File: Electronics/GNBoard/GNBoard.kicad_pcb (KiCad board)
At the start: 2 copper layers, 77.9 x 54.5 mm, 47 parts, among them K1 IR1, K10 IR4, K11 CNY_1, K12 CNY_2, K13 CNY_3, K14 CNY_4, K15 CNY_5, K16 CNY_6, K2 IR2, K3 SERVO_1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

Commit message: Working in new version for the GNBoard
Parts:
- removed K15: CNY_5, PIN_ARRAY_3X1
- removed K16: CNY_6, PIN_ARRAY_3X1
- removed P5: I2C_2, PIN_ARRAY_4x1
- added K17: Nose, PIN_ARRAY_3X1, F.Cu at (125.9, 92.8)
- added M1: XBEE, xbee_r1-XBEE, F.Cu at (117.0, 50.9)
- added R13: 10k, R3-LARGE_PADS, F.Cu at (128.4, 100.5)
- added R14: 10k, R3-LARGE_PADS, F.Cu at (123.3, 100.5)
- added R15: 4k7, R3-LARGE_PADS, F.Cu at (120.1, 43.4)
- added R16: 4k7, R3-LARGE_PADS, F.Cu at (120.1, 46.1)
- added R17: 7k5, R3-LARGE_PADS, F.Cu at (120.1, 48.8)
- added R18: 99k, R3-LARGE_PADS, F.Cu at (65.8, 42.2)
- C1: footprint C1V5 -> C1V8
- L1: footprint Choke_Toroid_6,5x13mm_Vertical -> Choke_Toroid_8x16mm_Vertical
- LED1: footprint LED5_RGB_long_wide -> LED5_RGB_long
- R1: value 6k8 -> 62k
- R5: value 6k8 -> 20k
- SHIELD1: footprint ARDUINO_MEGA_SHIELD -> ARDUINO_MEGA_SHIELD_MOD
- SW1: footprint SWITCH_3Pin -> switch_power_custom
- moved C4 120.6 mm to (64.6, 47.1)
- moved C5 99.2 mm to (108.0, 35.1)
- moved C2 98.8 mm to (72.6, 57.4), turned to 90 degrees
- moved LED1 94.8 mm to (62.6, 37.5), turned to 0 degrees
- moved SW3 88.9 mm to (54.1, 73.3)
- moved R2 88.9 mm to (70.6, 33.0), turned to 180 degrees
- moved SW1 88.8 mm to (55.6, 62.4)
- moved K11 88.6 mm to (95.4, 36.7)
- moved K12 88.6 mm to (97.9, 36.7)
- moved K13 88.6 mm to (100.5, 36.7)
- moved K14 88.6 mm to (103.0, 36.7)
- moved D1 88.6 mm to (68.2, 63.5)
- moved SW2 88.1 mm to (55.8, 42.0)
- moved R11 87.3 mm to (120.1, 32.9)
- moved P1 87.3 mm to (55.8, 54.0)
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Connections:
- C5 pad 1: +5V -> +3.3V
- P3 pad 2: GND -> N-0000043
- P6 pad 3: N-0000082 -> (no net)
- SHIELD1 pad 13: N-0000067 -> (no net)
- SHIELD1 pad 18: CNY5 -> XB_DIN
- SHIELD1 pad 19: CNY6 -> XB_DOUT
- SHIELD1 pad 3V3: N-0000040 -> +3.3V
- SHIELD1 pad AD10: N-0000041 -> Nose_V
- SHIELD1 pad AD11: N-0000039 -> (no net)
- SHIELD1 pad AD12: N-0000042 -> (no net)
- SHIELD1 pad AD13: N-0000043 -> (no net)
- SHIELD1 pad AD14: N-0000044 -> (no net)
- SHIELD1 pad AD15: N-0000045 -> (no net)
- SHIELD1 pad AREF: N-0000037 -> (no net)
- SHIELD1 pad V_IN: N-0000038 -> (no net)
- SW1 pad 3: N-0000046 -> (no net)
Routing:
- net GND: track 352.1 -> 36.9 mm, vias 4 -> 0
- net +5V: track 208.7 -> 43.3 mm
- net LDR4: track 39.0 -> 0.00 mm
- net LDR3: track 36.5 -> 0.00 mm
- net LDR2: track 33.9 -> 0.00 mm
- net XB_DOUT: track 0.00 -> 31.8 mm
- net LDR1: track 31.4 -> 0.00 mm
- net XB_DIN: track 0.00 -> 28.3 mm
- net BattVolt: track 44.8 -> 18.7 mm
- net +3.3V: track 0.00 -> 18.8 mm
- net Button1: track 5.50 -> 21.8 mm
- net ResetB: track 5.13 -> 20.8 mm
- net DHTpin: track 14.1 -> 0.00 mm
- net +BATT: track 28.9 -> 40.5 mm
- net N-0000034: track 0.00 -> 11.2 mm
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- added copper zone on F.Cu, net +5V
- added copper zone on B.Cu, net GND
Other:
- board size 77.9 x 54.5 mm -> 80 x 55.9 mm
- net class Default: clearance 0.4 -> 0.3; trace_width 0.8 -> 0.4; via_dia 1.5 -> 0.889; via_drill 0.6 -> 0.508
- rule trace_clearance: 0.4 -> 0.3
- board text added: "GNBoard v0.2"
- board text removed: "GNBoard"
- board text removed: "v0.1"

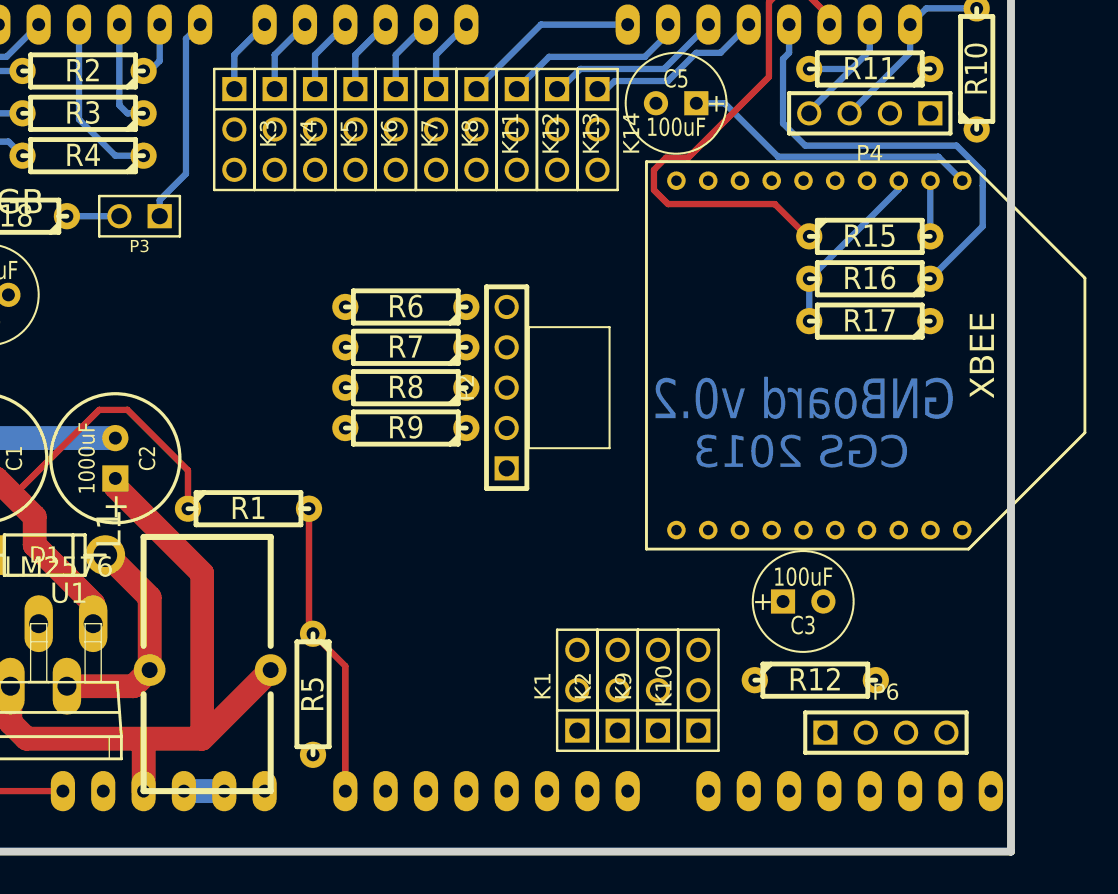
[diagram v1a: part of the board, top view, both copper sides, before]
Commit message: Added support for LDRs, lots of changes
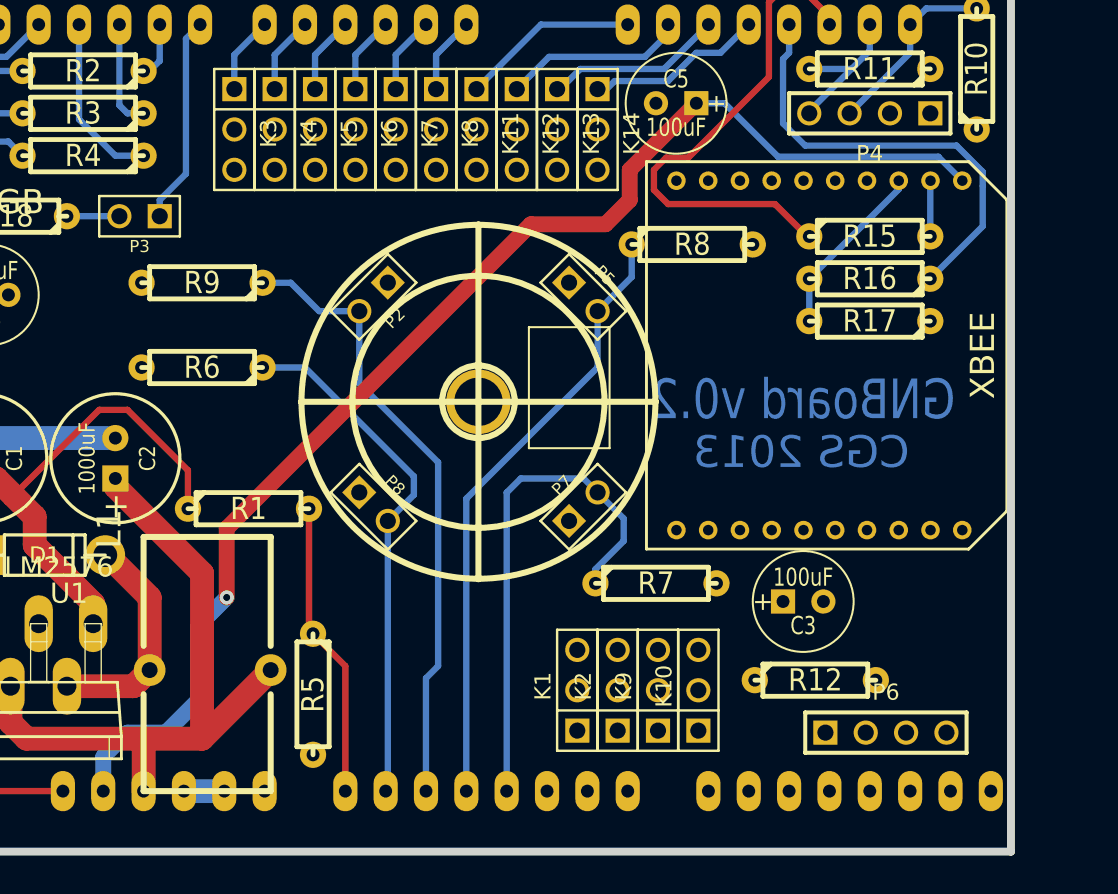
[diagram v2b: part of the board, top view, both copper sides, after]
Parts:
- added 1PIN: P***, ldr_drill, F.Cu at (95.5, 53.8)
- added P5: LDR_2, PIN_ARRAY_2X1, F.Cu at (102.1, 47.2)
- added P7: LDR_3, PIN_ARRAY_2X1, F.Cu at (102.1, 60.5)
- added P8: LDR_4, PIN_ARRAY_2X1, F.Cu at (88.9, 60.5)
- P2: value CONN_5 -> LDR_1; footprint PIN_ARRAY_5x1 -> PIN_ARRAY_2X1
- moved R7 21.7 mm to (106.7, 65.3), turned to 0 degrees
- moved R8 20.2 mm to (109.0, 43.9), turned to 0 degrees
- moved R9 15.8 mm to (78.1, 46.4)
- moved R6 13.4 mm to (78.1, 51.7)
- moved P2 10.1 mm to (88.9, 47.2), turned to 225 degrees
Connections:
- SHIELD1 pad AD1: LDR1 -> LDR4
- SHIELD1 pad AD2: LDR2 -> LDR1
- SHIELD1 pad AD3: LDR3 -> LDR2
- SHIELD1 pad AD4: LDR4 -> LDR3
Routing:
- net +3.3V: track 18.8 -> 81.7 mm, vias 0 -> 1
- net LDR1: track 0.00 -> 39.4 mm
- net LDR2: track 0.00 -> 38.7 mm
- net LDR4: track 0.00 -> 32.9 mm
- net LDR3: track 0.00 -> 32.4 mm

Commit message: Finished preliminary design
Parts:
- P1: value Battery -> Pwr
- SHIELD1: footprint ARDUINO_MEGA_SHIELD_MOD -> ARDUINO_MEGA_SHIELD_040pins_MOD
- moved R14 28.8 mm to (124.0, 71.6), turned to 0 degrees
- moved R9 27.4 mm to (90.9, 70.6), turned to 90 degrees
- moved R6 21.5 mm to (88.3, 70.6), turned to 90 degrees
- moved C4 16.0 mm to (80.6, 46.7)
- moved R7 11.9 mm to (96.0, 70.6), turned to 90 degrees
- moved C3 10.3 mm to (126.2, 66.8), turned to 90 degrees
- moved R12 6.81 mm to (118.4, 64.8)
- moved K1 2.95 mm to (98.8, 71.6)
- moved K9 2.95 mm to (103.9, 71.6)
- moved K10 2.95 mm to (106.4, 71.6)
- moved K2 2.95 mm to (101.3, 71.6)
- moved P6 2.81 mm to (124.0, 74.4)
- moved R8 0.80 mm to (109.2, 44.7)
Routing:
- net LDR4: track 32.9 -> 20.3 mm
- net LDR3: track 32.4 -> 24.7 mm
- net V_IR4: track 0.00 -> 6.63 mm
- net LDR1: track 39.4 -> 33.7 mm
- net V_IR3: track 0.00 -> 4.61 mm
- net V_IR1: track 0.00 -> 4.61 mm
- net V_IR2: track 0.00 -> 4.61 mm
- net GND: track 36.9 -> 38.5 mm
- net +5V: track 43.3 -> 42.2 mm
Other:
- board size 80 x 55.9 mm -> 80.8 x 55.4 mm
- board text added: "+"
- board text added: "- +"
- board text added: "14"
- board text added: "15"
- board text added: "16"
- board text added: "17"
- board text added: "2"
- board text added: "3"
- board text added: "4"
- board text added: "5"
- board text added: "5V"
- board text added: "5v"
- board text added: "6"
- board text added: "7"
- board text added: "A5"
- board text added: "A6"
- board text added: "A7"
- board text added: "A8"
- board text added: "CGS 2014"
- board text added: "DHT"
- board text added: "G"
- board text added: "GNBoard"
- board text added: "GND"
- board text added: "Gnd"
- board text added: "Nose"
- board text added: "Off On"
- board text added: "P1"
- board text added: "Pwm"
- board text added: "Reset"
- board text added: "SCL"
- board text added: "SDA"
- board text added: "d"
- board text removed: "CGS 2013"

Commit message: Finished v1.0 of the GNBoard
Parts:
- removed K17: Nose, PIN_ARRAY_3X1
- removed K8: SERVO_6, PIN_ARRAY_3X1
- added P10: Nose_Heater, PIN_ARRAY_2X1, F.Cu at (125.7, 72.4)
- added P11: CONN_1, PIN_ARRAY_1, F.Cu at (124.5, 69.8)
- added P9: Nose_Sense, PIN_ARRAY_2X1, F.Cu at (125.7, 74.9)
- added Q1: NPN, TO92-123, F.Cu at (125.5, 64.5)
- P1: value Pwr -> Battery
- R18: value 99k -> 47
- moved R13 51.4 mm to (112.5, 51.6), turned to 0 degrees
- moved R14 18.6 mm to (106.2, 66.0)
- moved P6 8.39 mm to (115.6, 74.2)
- moved C3 7.96 mm to (118.6, 69.1), turned to 270 degrees
- moved C5 3.56 mm to (111.5, 35.1), turned to 90 degrees
- moved K12 2.54 mm to (95.4, 36.7)
- moved K14 2.54 mm to (100.5, 36.7)
- moved K11 2.54 mm to (92.8, 36.7)
- moved K13 2.54 mm to (97.9, 36.7)
- moved R12 2.05 mm to (116.3, 64.5), turned to 180 degrees
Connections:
- net Nose_V renamed Nose_Vout
- R13 pad 1: (no net) -> Nose_heat
- R14 pad 1: +5V -> GND
- SHIELD1 pad 2: Servo6 -> Nose_heat
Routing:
- net Nose_heat: track 0.00 -> 29.7 mm, vias 0 -> 2
- net N-0000037: track 0.00 -> 27.6 mm, vias 0 -> 1
- net Nose_Vout: track 0.00 -> 24.4 mm, vias 0 -> 1
- net DHTpin: track 0.00 -> 16.8 mm, vias 0 -> 1
- net N-0000038: track 0.00 -> 10.5 mm
- net Servo6: track 4.85 -> 0.00 mm
- net CNY4: track 11.2 -> 13.7 mm
- net CNY3: track 11.2 -> 13.7 mm
- net CNY1: track 11.2 -> 13.7 mm
- net CNY2: track 11.5 -> 13.7 mm
- net GND: track 38.5 -> 36.9 mm
- net +3.3V: track 81.7 -> 80.7 mm, vias 1 -> 3
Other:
- outline, holes or cut-outs redrawn
- board text added: "2N2222"
- board text added: "A11"
- board text added: "A12"
- board text added: "A13"
- board text added: "A14"
- board text added: "A15"
- board text added: "A9"
- board text added: "DHT11"
- board text added: "EPS UAM"
- board text added: "GNBoard v1.0"
- board text added: "H+"
- board text added: "H-"
- board text added: "Max: 20V"
- board text added: "NC"
- board text added: "S+"
- board text added: "S-"
- board text added: "a"
- board text removed: "2"
- board text removed: "DHT"
- board text removed: "GNBoard v0.2"

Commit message: Finished v1.0 of the GNBoard
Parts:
- moved C1 5.92 mm to (65.5, 51.6)
- moved C2 5.92 mm to (73.9, 51.6)
- moved D1 5.92 mm to (69.4, 57.7)
- moved K1 5.92 mm to (100.0, 65.8)
- moved K10 5.92 mm to (107.6, 65.8)
- moved K11 5.92 mm to (94.1, 30.9)
- moved K12 5.92 mm to (96.6, 30.9)
- moved K13 5.92 mm to (99.1, 30.9)
- moved K14 5.92 mm to (101.7, 30.9)
- moved K2 5.92 mm to (102.6, 65.8)
- moved K3 5.92 mm to (81.4, 30.9)
- moved K5 5.92 mm to (86.4, 30.9)
- moved K6 5.92 mm to (89.0, 30.9)
- moved K7 5.92 mm to (91.5, 30.9)
- moved K9 5.92 mm to (105.1, 65.8)
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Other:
- board text added: "CC-BY-SA"
